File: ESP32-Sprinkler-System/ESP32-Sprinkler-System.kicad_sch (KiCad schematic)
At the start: 13 parts

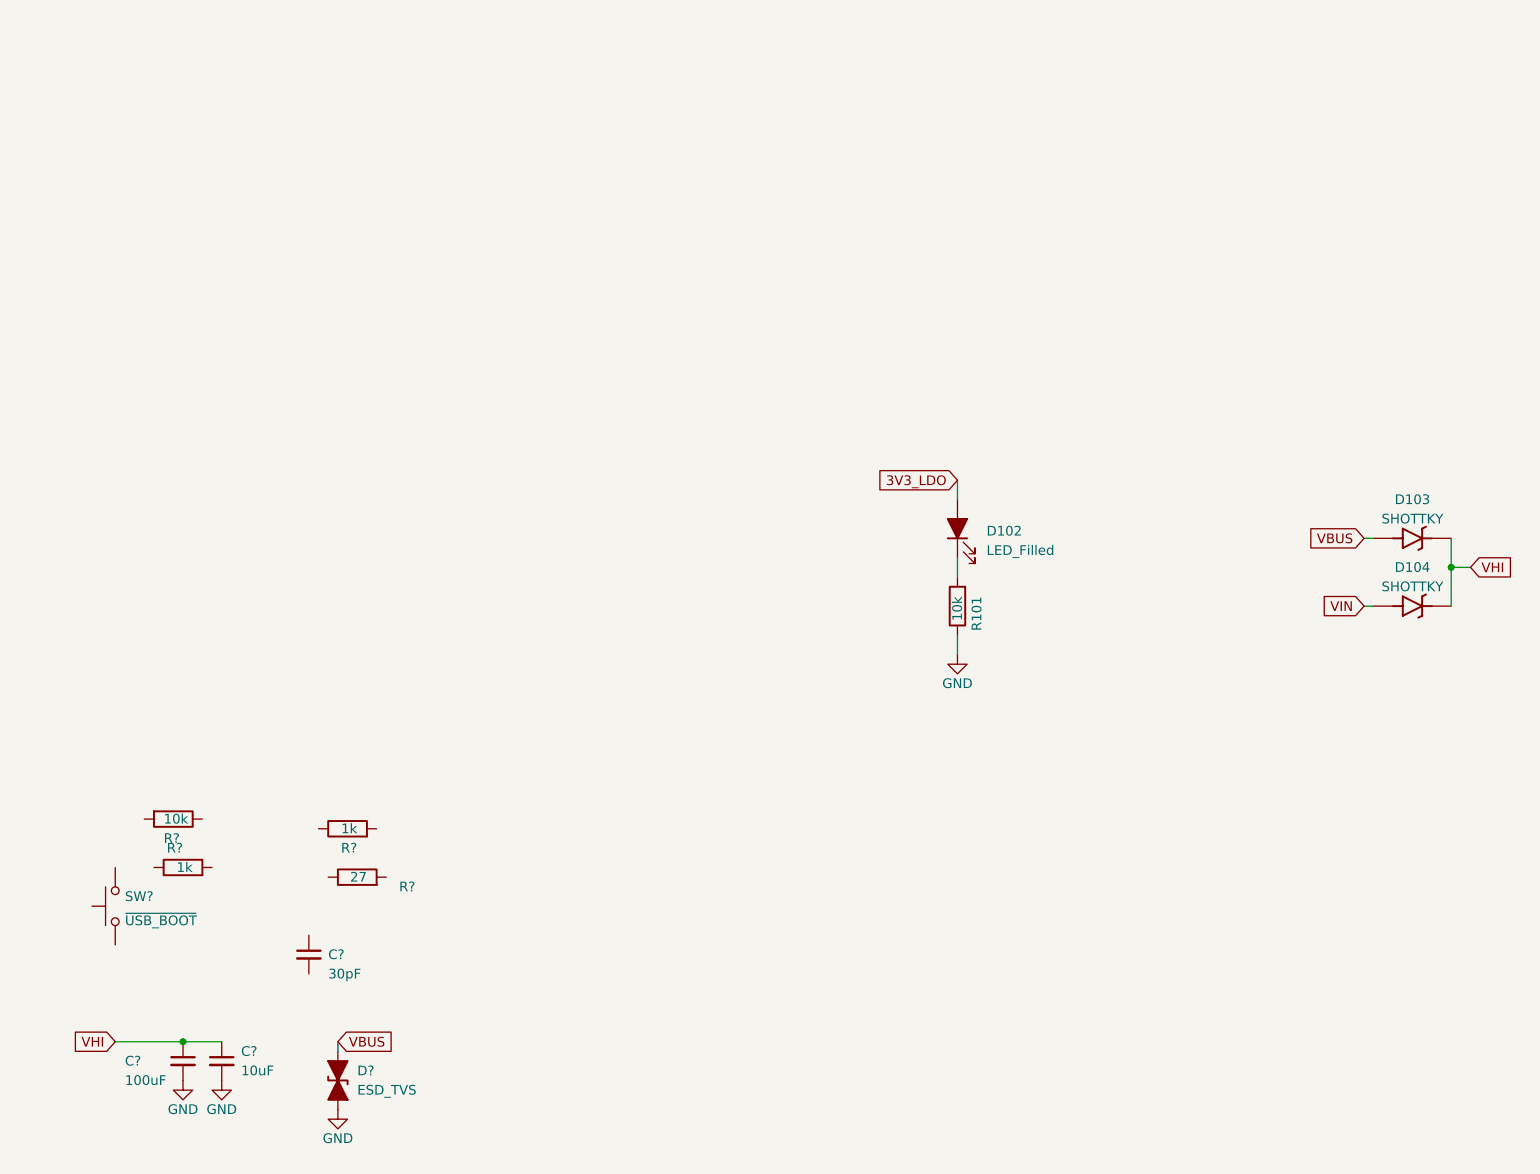
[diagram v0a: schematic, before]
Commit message: Created PCB File and got ESP32 files (sym,foot,step)
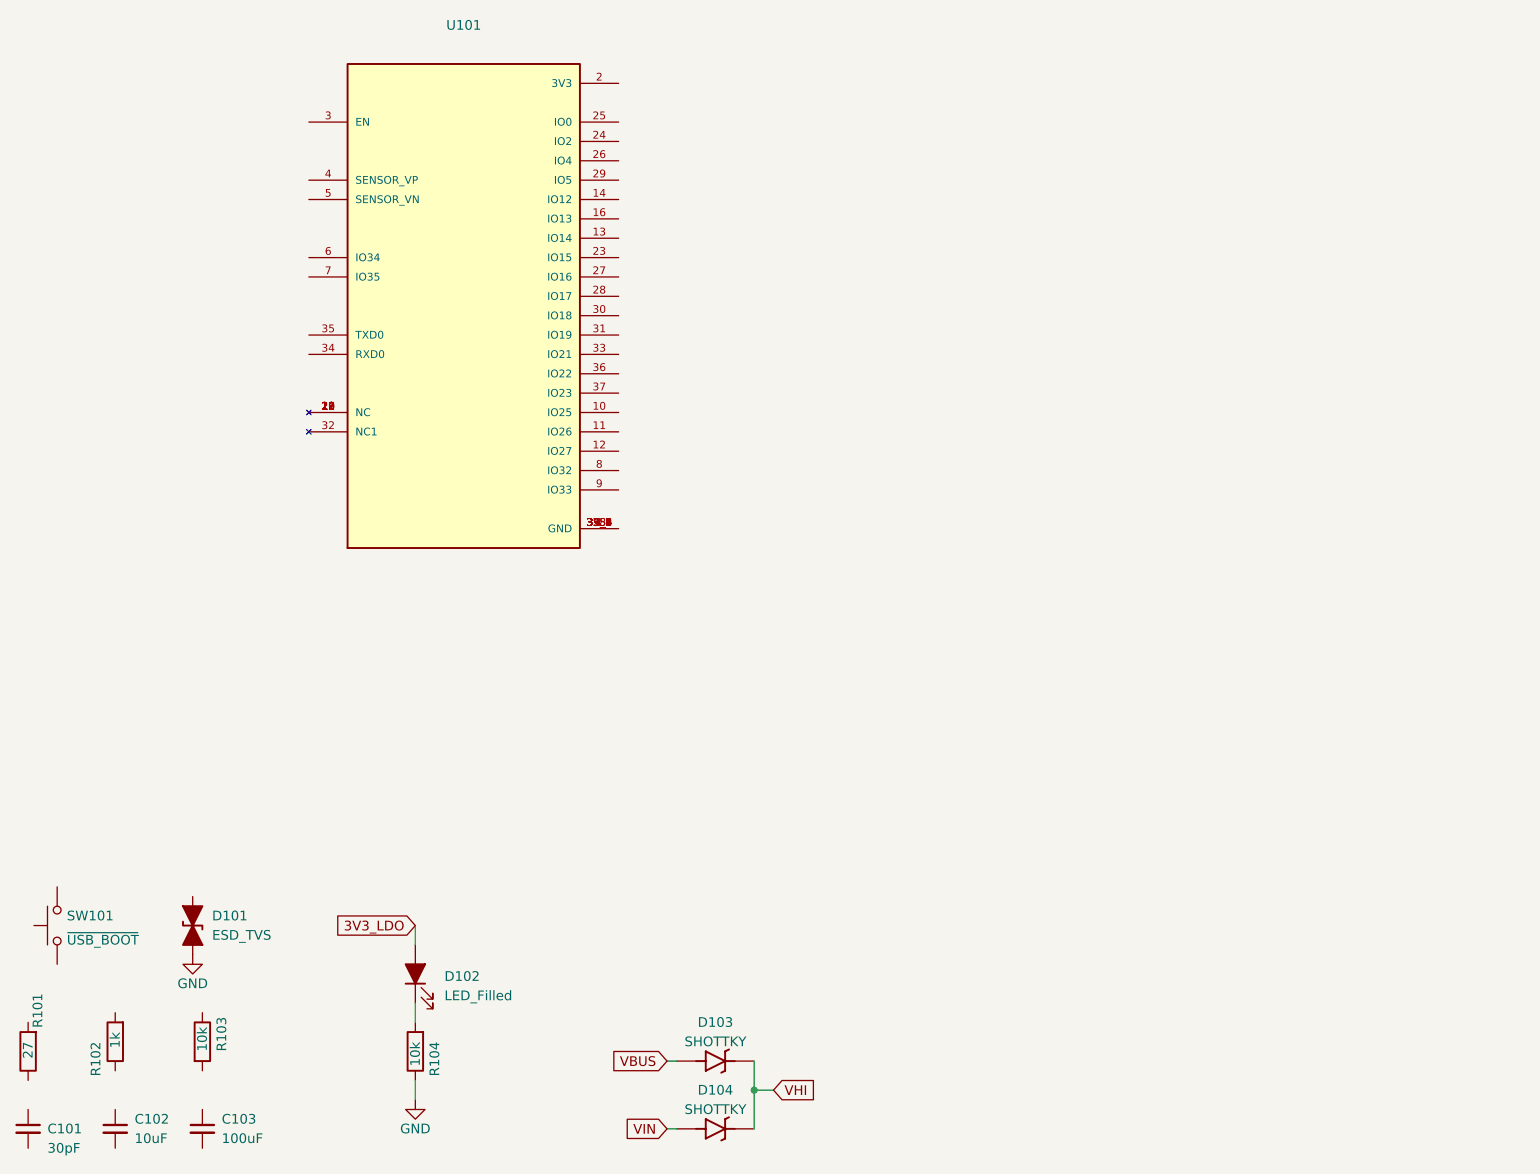
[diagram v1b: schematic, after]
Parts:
- removed R?: 1k, Breadstick Footprints:Perfect_0402_Resistor, symbol Device:R
- added U101: (no value), symbol ESP32-WROOM-32E__16MB_:ESP32-WROOM-32E_(16MB)
- gave numbers to parts that had none: 8
- renumbered R101 to R104
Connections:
- net GND: no longer C102.2, C103.2
- net VBUS: no longer D101.2 (A2)
- net VHI: no longer C102.1, C103.1
- new net: U101.1 (GND), U101.15 (GND), U101.38 (GND), U101.39_1 (GND), U101.39_2 (GND), U101.39_3 (GND), U101.39_4 (GND), U101.39_5 (GND), U101.39_6 (GND), U101.39_7 (GND), U101.39_8 (GND), U101.39_9 (GND)
- new net: U101.17 (NC), U101.18 (NC), U101.19 (NC), U101.20 (NC), U101.21 (NC), U101.22 (NC)
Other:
- moved on the sheet: C101, C102, C103, D101, D102, D103, D104, R101, R102, R103, R104, SW101

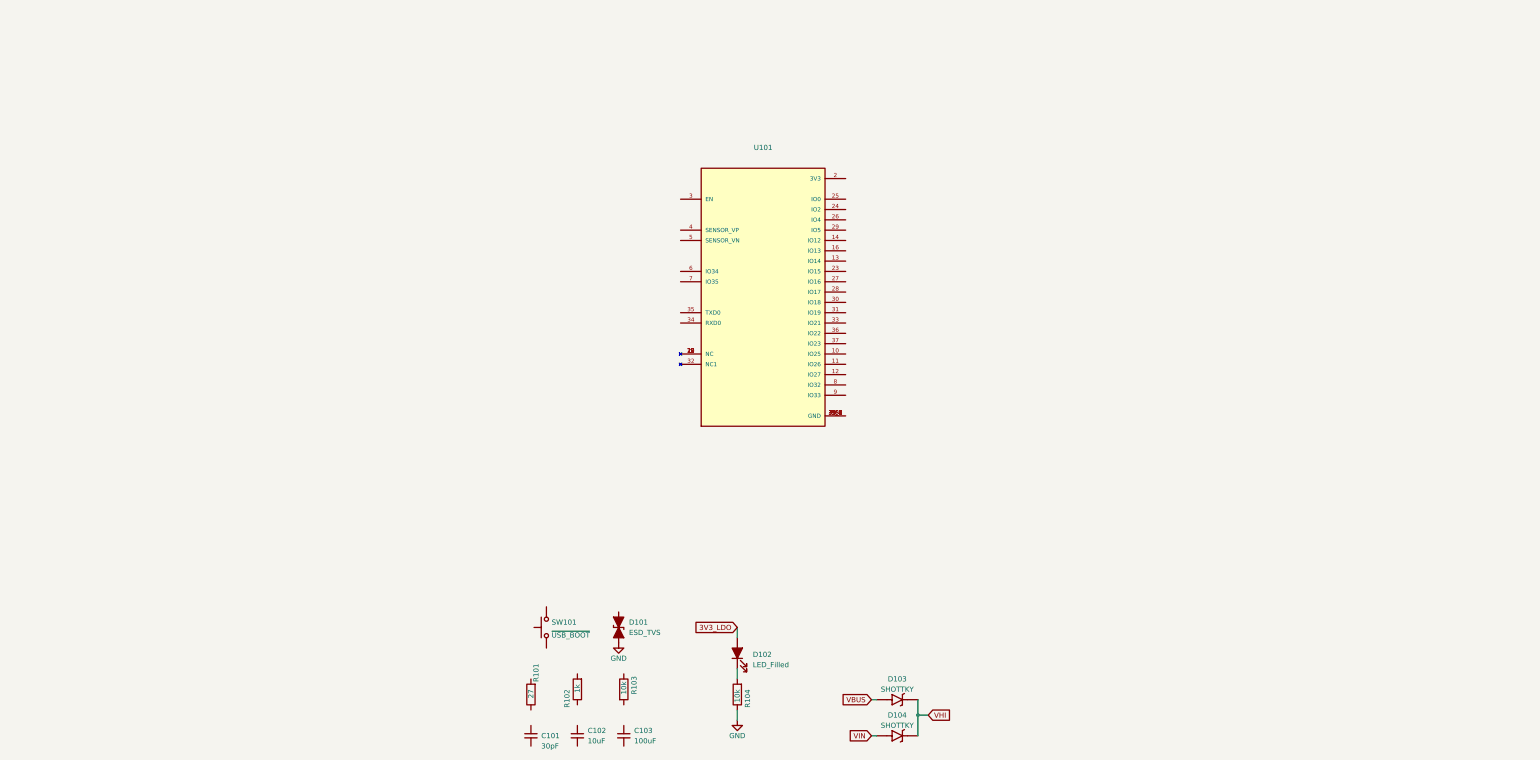
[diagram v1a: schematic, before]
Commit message: 3D models for most of the components.
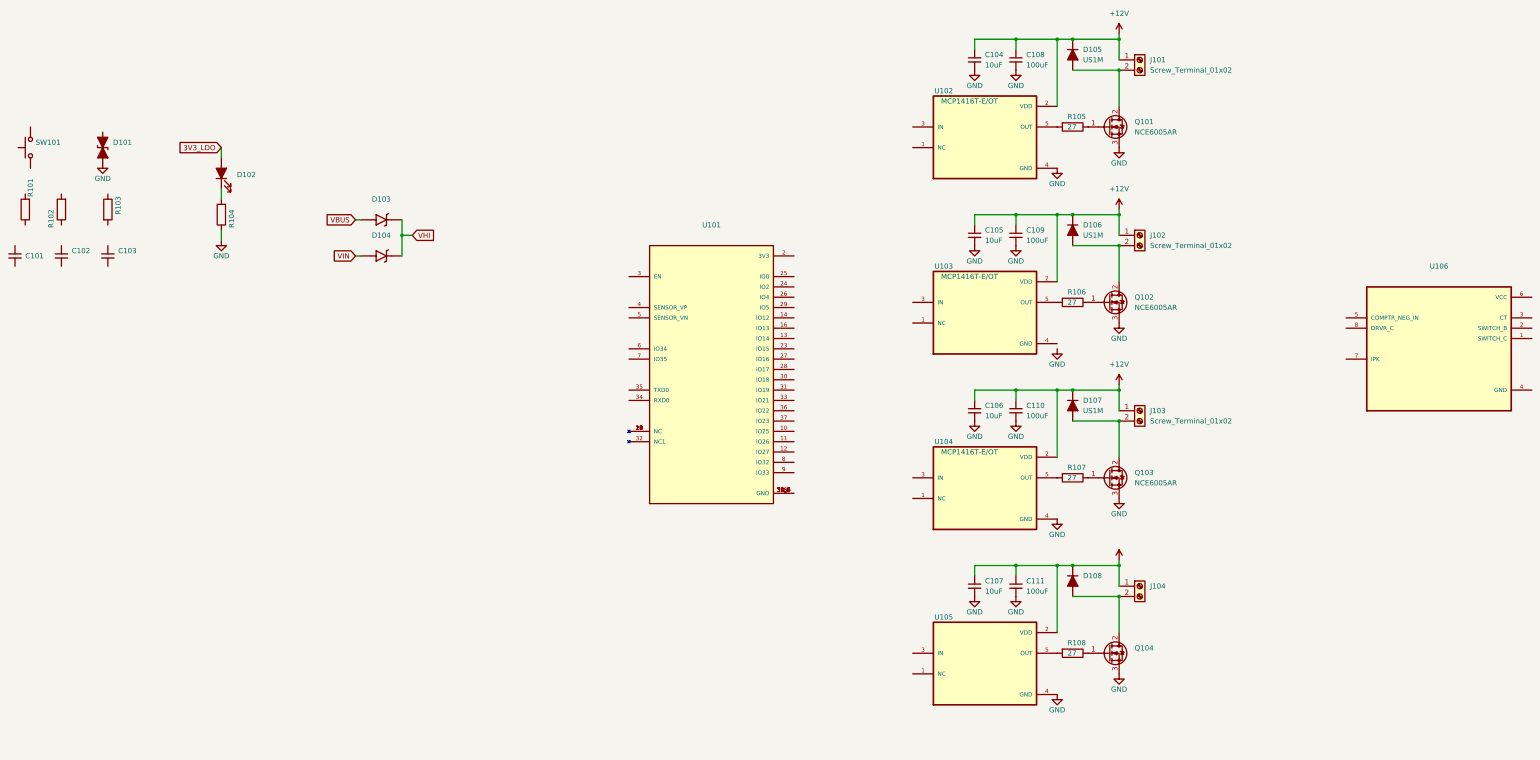
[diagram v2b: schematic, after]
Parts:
- added C104, C105, C106, C107: 10uF, Breadstick Footprints:Perfect_0402_Cap, symbol Device:C_Small
- added C108, C109, C110, C111: 100uF, Capacitor_SMD:C_1206_3216Metric, symbol Device:C_Small
- added D105, D106, D107: US1M, Diode_SMD:D_SMA, symbol Device:D_Filled
- added D108: (no value), symbol Device:D_Filled
- added J101, J102, J103: Screw_Terminal_01x02, Breadstick Footprints:KF202-50-2P, symbol Connector:Screw_Terminal_01x02
- added J104: (no value), symbol Connector:Screw_Terminal_01x02
- added Q101, Q102, Q103: NCE6005AR, Package_TO_SOT_SMD:SOT-223-3_TabPin2, symbol Transistor_FET:BSP89
- added Q104: (no value), symbol Transistor_FET:BSP89
- added R105, R106, R107, R108: 27, Breadstick Footprints:Perfect_0402_Resistor, symbol Device:R
- added U102, U103, U104: MCP1416T-E/OT, MCP1416T-E_OT:SOT95P270X145-5N, symbol MCP1416T-E_OT:MCP1416T-E/OT
- added U105: (no value), symbol MCP1416T-E_OT:MCP1416T-E/OT
- added U106: (no value), symbol MC34063AD:MC34063AD
- C101: value 30pF -> (none); footprint Breadstick Footprints:Perfect_0402_Cap -> (none)
- C102: value 10uF -> (none); footprint Breadstick Footprints:Perfect_0402_Cap -> (none)
- C103: value 100uF -> (none); footprint Capacitor_SMD:C_1206_3216Metric -> (none)
- D101: value ESD_TVS -> (none); footprint Breadstick Footprints:Perfect_0402_Resistor -> (none)
- D102: value LED_Filled -> (none); footprint LED_SMD:LED_0805_2012Metric -> (none)
- D103, D104: value SHOTTKY -> (none); footprint Diode_SMD:D_SOD-123 -> (none)
- R101: value 27 -> (none); footprint Breadstick Footprints:Perfect_0402_Resistor -> (none)
- R102: value 1k -> (none); footprint Breadstick Footprints:Perfect_0402_Resistor -> (none)
- R103, R104: value 10k -> (none); footprint Breadstick Footprints:Perfect_0402_Resistor -> (none)
- SW101: value ~{USB_BOOT} -> (none); footprint Breadstick Footprints:GT-TC029B-H025-L1N -> (none)
- U101: JLCPCB P/N (none) -> C701343
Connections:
- net GND: now also C104.2, C105.2, C106.2, C107.2, C108.2, C109.2, C110.2, C111.2, Q101.3 (S), Q102.3 (S), Q103.3 (S), Q104.3 (S), U102.4 (GND), U104.4 (GND), U105.4 (GND)
- new net: Q101.1 (G), R105.1
- new net: D105.2 (A), J101.2 (Pin_2), Q101.2 (D)
- new net: R107.2, U104.5 (OUT)
- new net: Q103.1 (G), R107.1
- new net: D107.2 (A), J103.2 (Pin_2), Q103.2 (D)
- new net: R108.2, U105.5 (OUT)
- new net: R105.2, U102.5 (OUT)
- new net: D106.2 (A), J102.2 (Pin_2), Q102.2 (D)
- new net: Q104.1 (G), R108.1
- new net: D108.2 (A), J104.2 (Pin_2), Q104.2 (D)
- new net: Q102.1 (G), R106.1
- new net: R106.2, U103.5 (OUT)
- new net +12V: C104.1, C105.1, C106.1, C107.1, C108.1, C109.1, C110.1, C111.1, D105.1 (K), D106.1 (K), D107.1 (K), D108.1 (K), J101.1 (Pin_1), J102.1 (Pin_1), J103.1 (Pin_1), J104.1 (Pin_1), U102.2 (VDD), U103.2 (VDD), U104.2 (VDD), U105.2 (VDD)
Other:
- moved on the sheet: C101, C102, C103, D101, D102, D103, D104, R101, R102, R103, R104, SW101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

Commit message: Need caps that can handle 12V
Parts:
- removed C104, C105, C106, C107: 10uF, Breadstick Footprints:Perfect_0402_Cap, symbol Device:C_Small
- removed C108, C109, C110, C111: 100uF, Capacitor_SMD:C_1206_3216Metric, symbol Device:C_Small
- removed D105, D106, D107: US1M, Diode_SMD:D_SMA, symbol Device:D_Filled
- removed J101, J102, J103: Screw_Terminal_01x02, Breadstick Footprints:KF202-50-2P, symbol Connector:Screw_Terminal_01x02
- removed Q101, Q102, Q103: NCE6005AR, Package_TO_SOT_SMD:SOT-223-3_TabPin2, symbol Transistor_FET:BSP89
- removed R105, R106, R107: 27, Breadstick Footprints:Perfect_0402_Resistor, symbol Device:R
- removed U102, U103, U104: MCP1416T-E/OT, MCP1416T-E_OT:SOT95P270X145-5N, symbol MCP1416T-E_OT:MCP1416T-E/OT
- added L?: (no value), symbol Device:L_Ferrite
- added R112: 1k, Breadstick Footprints:Perfect_0402_Resistor, symbol Device:R
- added R116: 27, Breadstick Footprints:Perfect_0402_Resistor, symbol Device:R
- C101: value (none) -> 30pF; footprint (none) -> Breadstick Footprints:Perfect_0402_Cap
- C102: value (none) -> 10uF; footprint (none) -> Breadstick Footprints:Perfect_0402_Cap
- C103: value (none) -> 100uF; footprint (none) -> Capacitor_SMD:C_1206_3216Metric
- D101: value (none) -> ESD_TVS; footprint (none) -> Breadstick Footprints:Perfect_0402_Resistor
- D102: value (none) -> LED_Filled; footprint (none) -> LED_SMD:LED_0805_2012Metric
- D103, D104: value (none) -> SHOTTKY; footprint (none) -> Diode_SMD:D_SOD-123
- D108: value (none) -> US1M; footprint (none) -> Diode_SMD:D_SMA
- J104: value (none) -> Screw_Terminal_01x02; footprint (none) -> Breadstick Footprints:KF202-50-2P
- Q104: value (none) -> NCE6005AR; footprint (none) -> Package_TO_SOT_SMD:SOT-223-3_TabPin2
- R101: value (none) -> 27; footprint (none) -> Breadstick Footprints:Perfect_0402_Resistor
- R102: value (none) -> 1k; footprint (none) -> Breadstick Footprints:Perfect_0402_Resistor
- R103, R104: value (none) -> 10k; footprint (none) -> Breadstick Footprints:Perfect_0402_Resistor
- R108: value 27 -> 10k; JLCPCB P/N C25100 -> C25744
- SW101: value (none) -> ~{USB_BOOT}; footprint (none) -> Breadstick Footprints:GT-TC029B-H025-L1N
- U101: value (none) -> ESP32-WROOM-32E_(16MB); footprint (none) -> ESP32-WROOM-32E__16MB_:XCVR_ESP32-WROOM-32E_(16MB)
- U105: value (none) -> MCP1416T-E/OT; footprint (none) -> MCP1416T-E_OT:SOT95P270X145-5N
- U106: value (none) -> MC34063AD; footprint (none) -> MC34063AD:SOIC127P599X175-8N
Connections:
- net GND: now also R108.2
- net at U105.3 (IN): now also R112.1
- net at U105.5 (OUT): now also R116.2; no longer R108.2
- net at Q104.1 (G): now also R116.1; no longer R108.1
- new net: R108.1, R112.2
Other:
- note added: "Find Capacitors that can handle 12V"
- moved on the sheet: U106

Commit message: Continued work on schematic
Completed solenoid drivers.
Working on Buck Converter.
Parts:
- removed D108: US1M, Diode_SMD:D_SMA, symbol Device:D_Filled
- removed J104: Screw_Terminal_01x02, Breadstick Footprints:KF202-50-2P, symbol Connector:Screw_Terminal_01x02
- removed Q104: NCE6005AR, Package_TO_SOT_SMD:SOT-223-3_TabPin2, symbol Transistor_FET:BSP89
- removed R108: 10k, Breadstick Footprints:Perfect_0402_Resistor, symbol Device:R
- removed R112: 1k, Breadstick Footprints:Perfect_0402_Resistor, symbol Device:R
- removed R116: 27, Breadstick Footprints:Perfect_0402_Resistor, symbol Device:R
- removed U105: MCP1416T-E/OT, MCP1416T-E_OT:SOT95P270X145-5N, symbol MCP1416T-E_OT:MCP1416T-E/OT
- added C104, C113: 220uF, Capacitor_SMD:CP_Elec_10x10, symbol Device:C_Polarized_US
- added C105, C106, C111, C112: 22uF, Capacitor_SMD:C_1206_3216Metric, symbol Device:C
- added C107, C108, C109, C110: 10uF, Capacitor_SMD:C_0603_1608Metric, symbol Device:C
- added D105: SS54, Diode_SMD:D_SMA, symbol Device:D_Filled
- L101: renamed from L?; value (none) -> L_Ferrite
- renumbered U106 to U102
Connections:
- net +12V: now also U102.6 (VCC), C104.1, C105.1, C106.1, C107.1, C108.1
- net GND: now also U102.4 (GND), C104.2, C105.2, C106.2, C107.2, C108.2, C109.2, C110.2, C111.2, C112.2, C113.2, D105.2 (A)
- net at U102.1 (SWITCH_C): now also U102.7 (IPK), U102.8 (DRVR_C)
- net at U102.2 (SWITCH_B): now also L101.1, D105.1 (K)
- net +3V3: now reaches L101.2
- net +3V3: now also C109.1, C110.1, C111.1, C112.1, C113.1
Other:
- added sheet Solenoid_Drivers (Solenoid_Drivers.kicad_sch)
- note added: "Run calculations from datasheet for final components."
- note removed: "Find Capacitors that can handle 12V"
- moved on the sheet: C102, L101, U101, U102

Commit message: Continued working on schematic
finished solenoid drivers, finished buck converter, started ESP32
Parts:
- removed C104, C113: 220uF, Capacitor_SMD:CP_Elec_10x10, symbol Device:C_Polarized_US
- removed C105, C106, C111, C112: 22uF, Capacitor_SMD:C_1206_3216Metric, symbol Device:C
- removed C107, C108, C109, C110: 10uF, Capacitor_SMD:C_0603_1608Metric, symbol Device:C
- removed D105: SS54, Diode_SMD:D_SMA, symbol Device:D_Filled
- removed L101: L_Ferrite, symbol Device:L_Ferrite
- removed U102: MC34063AD, MC34063AD:SOIC127P599X175-8N, symbol MC34063AD:MC34063AD
- added C102: (no value), symbol Device:C_Small
- added C104: 10uF, Breadstick Footprints:Perfect_0402_Cap, symbol Device:C_Small
- added J101: (no value), symbol Connector_Generic:Conn_01x06
- added R104: 10k, Breadstick Footprints:Perfect_0402_Resistor, symbol Device:R
- added U102: CH340C, CH340C:SOIC127P600X180-16N, symbol CH340C:CH340C
- SW101: value ~{USB_BOOT} -> (none)
- renumbered C102 to C103, C103 to C105, R103 to R101, R104 to R102, R102 to R103, R101 to R105
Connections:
- net +3V3: now also C103.1, C105.1, U101.2 (3V3), C104.1, J101.1 (Pin_1), R104.2
- net GND: now also C103.2, C105.2, SW101.1, U101.1 (GND), U101.15 (GND), U101.38 (GND), U101.39_1 (GND), U101.39_2 (GND), U101.39_3 (GND), U101.39_4 (GND), U101.39_5 (GND), U101.39_6 (GND), U101.39_7 (GND), U101.39_8 (GND), U101.39_9 (GND), C102.2, C104.2, J101.6 (Pin_6), U102.1 (GND)
- net at SW101.2: now also R105.2, R104.1
- net at R105.1: now also U101.3 (EN), C102.1
- net TMS: now reaches U101.13 (IO14)
- net TMS: now also J101.2 (Pin_2)
- net TDI: now reaches U101.14 (IO12)
- net TDI: now also J101.3 (Pin_3)
- net TCK: now reaches U101.16 (IO13)
- net TCK: now also J101.4 (Pin_4)
- net TDO: now reaches U101.23 (IO15)
- net TDO: now also J101.5 (Pin_5)
- net at U101.34 (RXD0): now also U102.2 (TXD)
- net at U101.35 (TXD0): now also U102.3 (RXD)
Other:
- added sheet BuckConverter (BuckConverter.kicad_sch)
- note added: "JTAG"
- note added: "UART"
- note removed: "Run calculations from datasheet for final components."
- moved on the sheet: C103, C105, R103, R105, SW101, U101
